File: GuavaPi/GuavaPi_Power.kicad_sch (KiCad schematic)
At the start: 1 part

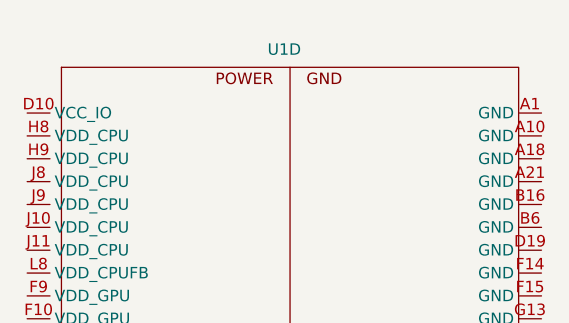
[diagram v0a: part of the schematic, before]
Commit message: Started DRAM Design
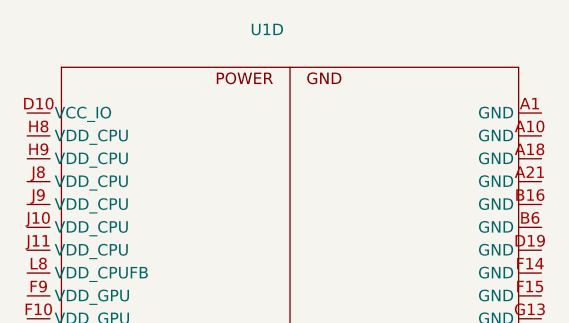
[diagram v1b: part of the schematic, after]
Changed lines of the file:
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@@
   (symbol (lib_id "Allwinner_H616:Allwinner_H616") (at 17.272 19.558 0) (unit 4)
     (in_bom yes) (on_board yes) (dnp no) (fields_autoplaced)
-    (property "Reference" "U1" (at 56.007 23.9268 0)
+    (property "Reference" "U1" (at 54.102 21.7424 0)
       (effects (font (size 1.27 1.27)))
     )
@@
           (reference "U1") (unit 4)
         )
+        (path "/3be7235b-2d12-456d-bbdb-dcc9c2ae1afd/dc1a4d83-a933-4336-ba01-88286996a5dc"
+          (reference "U1") (unit 4)
+        )

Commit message: AXP313A
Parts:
- added C38, C39, C40, C42, C45: 4.7uF, symbol Device:C
- added C41: 1uF, symbol Device:C
- added C43, C44, C46, C47, C48, C49, C50: 22uF, symbol Device:C
- added L1, L2, L3: 1uH, symbol Device:L
- added R10, R11, R12, R13: 2k, symbol Device:R
- added R9: 510R, symbol Device:R
- added UP1: ~, symbol allwinner_h616:AXP313A
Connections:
- new net: C40.2, R9.1, UP1.7 (RTCLCO)
- new net: L1.1, UP1.18 (LX1)
- new net: R12.1, UP1.11 (IRQ)
- new net: L2.1, UP1.19 (LX2)
- new net: C41.2, UP1.8 (GPO)
- new net: C42.1, UP1.17 (VIN1)
- new net: R13.1, UP1.13 (PWROK)
- new net 1V8: C38.2, R10.2, R11.2, UP1.15 (ALDO1)
- new net 3V3: C39.2, UP1.12 (DLDO1)
- new net GND: C38.1, C39.1, C40.1, C41.1, C42.2, C43.2, C44.2, C45.2, C46.2, C47.2, C48.2, C49.2, C50.2, R9.2, UP1.21 (EPAD), UP1.4 (GND)
- new net IRQ: R12.2
- new net PMU_SCK: R11.1, UP1.6 (SCL)
- new net PMU_SDA: R10.1, UP1.5 (SDA)
- new net PS: C45.1, C48.1, UP1.20 (VIN2)
- new net RESET: R13.2
- new net VCC_DRAM: C49.1, C50.1, L3.2
- new net VDD_CPU: C46.1, C47.1, L2.2, UP1.1 (DCDC2)
- new net VDD_GPU: C43.1, C44.1, L1.2, UP1.16 (DCDC1)
- no-connect marks 0 -> 2

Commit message: Power H616
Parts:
- added C51, C52, C53, C54, C55, C56, C57, C58, C59, C60, C61, C62, C63, C64, C65, C66, C67: 100nF, symbol Device:C
- added D1: LED, symbol Device:LED
- added D2: D, symbol Device:D
- added J1: 0533980271, MOLEX_0533980271, symbol 0533980271:0533980271
- added R14: 10k, symbol Device:R
- added R15: 5k1, symbol Device:R
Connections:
- net VCC_DRAM is gone; now on net VCC-DRAM: C49.1, C50.1, L3.2
- net VDD_CPU is gone; now on net VDD-CPU: C46.1, C47.1, L2.2, UP1.1 (DCDC2)
- net VDD_GPU is gone; now on net VDD-GPU: C43.1, C44.1, L1.2, UP1.16 (DCDC1)
- net 1V8: now also C52.2, C53.2, C54.2, R14.1
- net 3V3: now also C59.2, C60.2, C61.2, C62.2, R15.1
- net GND: now also U1.A1 (GND1), U1.A10 (GND2), U1.A18 (GND3), U1.A21 (GND4), U1.B16 (GND6), U1.B6 (GND5), U1.D19 (GND7), U1.F14 (GND8), U1.F15 (GND9), U1.G13 (GND10), U1.G14 (GND11), U1.G15 (GND12), U1.H10 (GND13), U1.H11 (GND14), U1.H12 (GND15), U1.H13 (GND16), U1.H14 (GND17), U1.H15 (GND18), U1.H19 (GND19), U1.J12 (GND20), U1.J13 (GND21), U1.J14 (GND22), U1.J15 (GND23), U1.K10 (GND26), U1.K11 (GND27), U1.K12 (GND28), U1.K13 (GND29), U1.K14 (GND30), U1.K15 (GND31), U1.K8 (GND24), U1.K9 (GND25), U1.L21 (GND32), U1.M1 (GND33), U1.M2 (GND34), U1.M3 (GND35), U1.N12 (GND38), U1.N15 (GND39), U1.N18 (GND40), U1.N6 (GND36), U1.N9 (GND37), U1.P3 (GND41), U1.R21 (GND43), U1.R5 (GND42), U1.T1 (GND44), U1.T10 (GND47), U1.T15 (GND48), U1.T17 (GND49), U1.T3 (GND45), U1.T8 (GND46), U1.U13 (GND51), U1.U6 (GND50), U1.V1 (GND52), U1.V12 (GND54), U1.V19 (GND55), U1.V21 (GND56), U1.V5 (GND53), C51.1, C52.1, C53.1, C54.1, C55.1, C56.1, C57.1, C58.1, C59.1, C60.1, C61.1, C62.1, C63.1, C64.1, C65.1, C66.1, C67.1, D1.1 (K), J1.2, J1.S1 (SHIELD), J1.S2 (SHIELD__1)
- net PS: now also UP1.2 (VIN3), D2.2 (A)
- net RESET: now also C51.2, R14.2
- net +3.3V: now reaches U1.D10 (VCC_IO)
- net VDD-GPU: now reaches U1.F10 (VDD_GPU2)
- net VDD-GPU: now also U1.F11 (VDD_SYS1), U1.F12 (VDD_SYS2), U1.F13 (VDD_SYS3), U1.F8 (VDD_GPUFB), U1.F9 (VDD_GPU1), U1.G10 (VDD_SYS4), U1.G11 (VDD_SYS5), U1.G12 (VDD_SYS6), U1.G8 (VDD_GPU3), U1.G9 (VDD_GPU4), C63.2, C64.2, C65.2
- net VDD-CPU: now reaches U1.H8 (VDD_CPU1)
- net VDD-CPU: now also U1.H9 (VDD_CPU2), U1.J10 (VDD_CPU5), U1.J11 (VDD_CPU6), U1.J8 (VDD_CPU3), U1.J9 (VDD_CPU4), U1.L8 (VDD_CPUFB), C66.2, C67.2
- net at UP1.3 (LX3): now also L3.1
- net VCC-DRAM: now reaches UP1.4 (GND)
- net VCC-DRAM: now also C55.2, C56.2, C57.2, C58.2
- new net: D2.1 (K), J1.1
- new net: D1.2 (A), R15.2

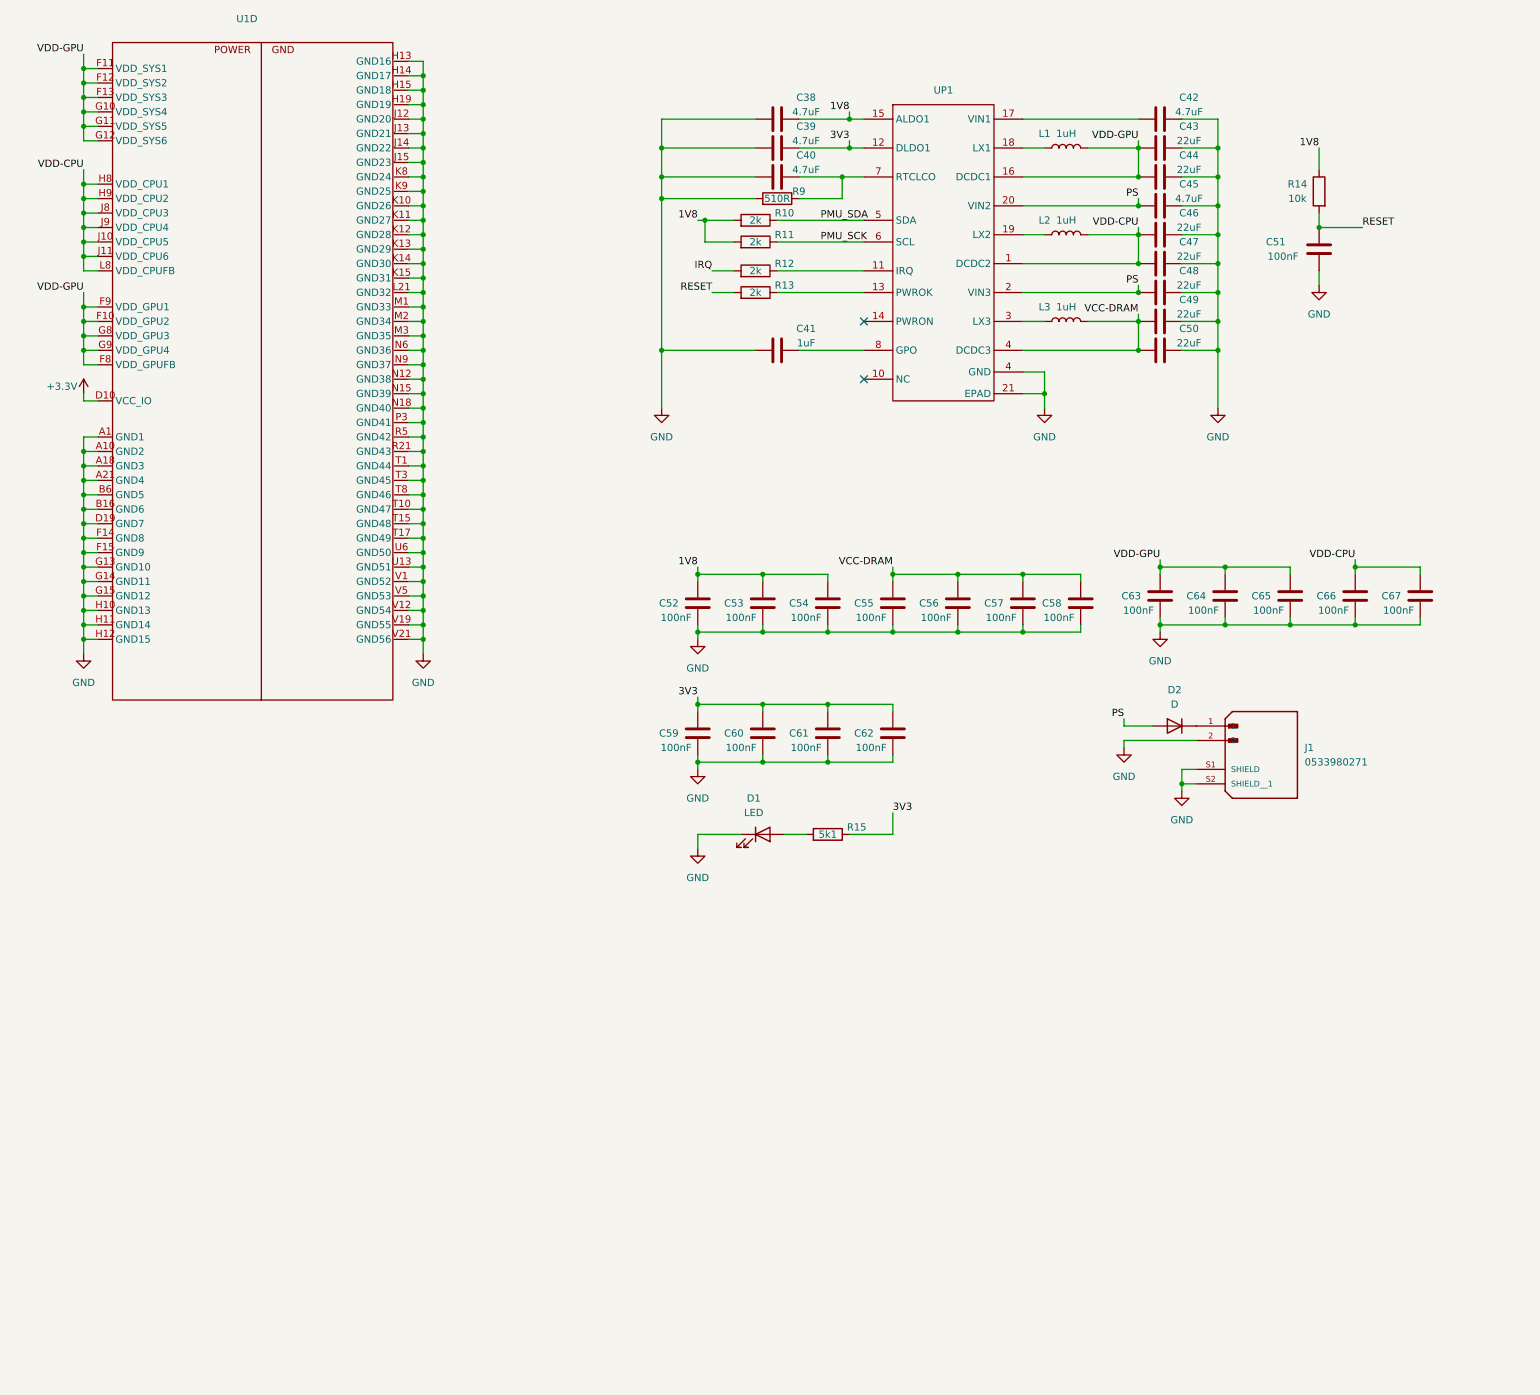
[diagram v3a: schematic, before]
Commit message: Added USB-C
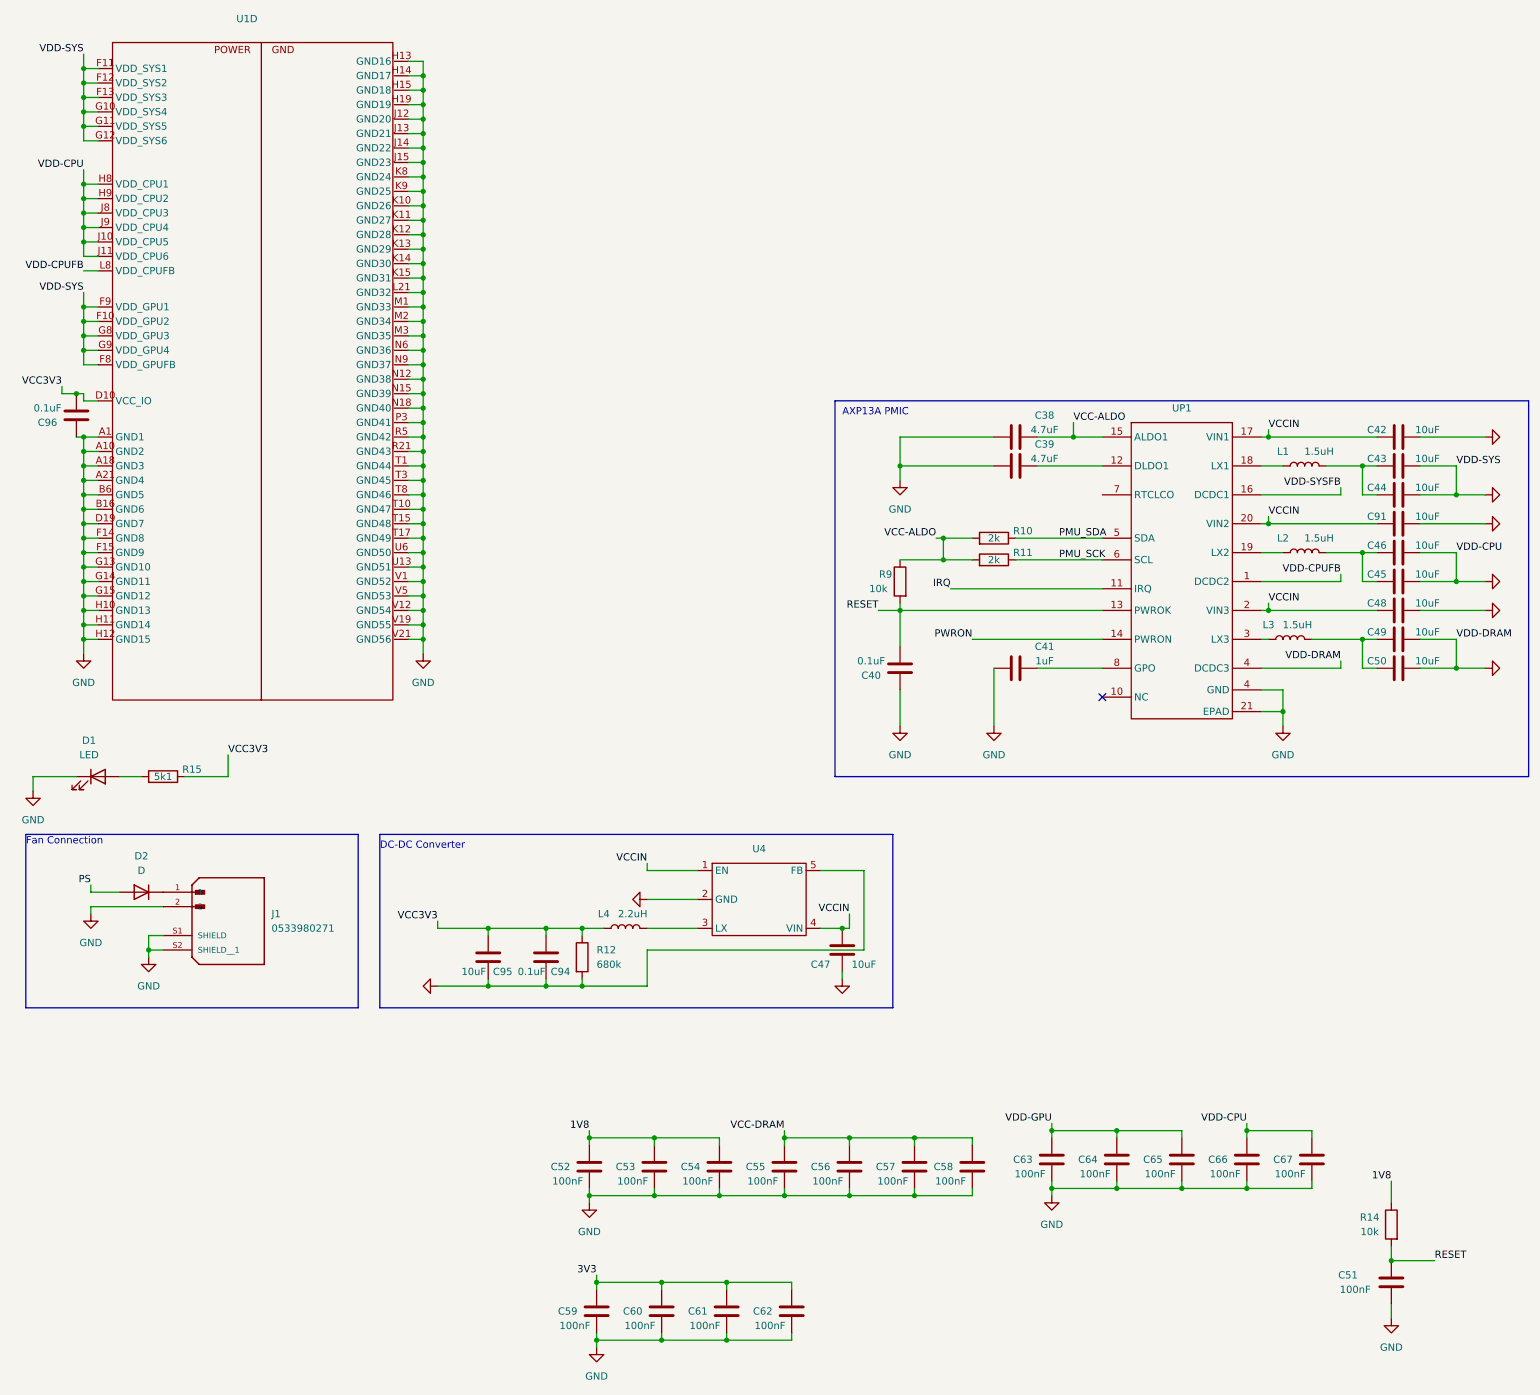
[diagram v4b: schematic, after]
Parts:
- removed R13: 2k, symbol Device:R
- added C91, C95: 10uF, symbol Device:C
- added C94, C96: 0.1uF, symbol Device:C
- added L4: 2.2uH, symbol Device:L
- added U4: ~, symbol Converter_DCDC:MT3410LB
- C40: value 4.7uF -> 0.1uF
- C42, C45: value 4.7uF -> 10uF
- C43, C44, C46, C47, C48, C49, C50: value 22uF -> 10uF
- L1, L2, L3: value 1uH -> 1.5uH
- R12: value 2k -> 680k
- R9: value 510R -> 10k
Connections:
- net +3.3V is gone; now on net VCC3V3: U1.D10 (VCC_IO)
- net 1V8: no longer C38.2, R10.2, R11.2, UP1.15 (ALDO1)
- net 3V3: no longer C39.2, R15.1, UP1.12 (DLDO1)
- net GND: now also C47.1, C66.2, C67.2, R12.2, U1.F10 (VDD_GPU2), U1.F11 (VDD_SYS1), U1.F12 (VDD_SYS2), U1.F13 (VDD_SYS3), U1.F8 (VDD_GPUFB), U1.F9 (VDD_GPU1), U1.G10 (VDD_SYS4), U1.G11 (VDD_SYS5), U1.G12 (VDD_SYS6), U1.G8 (VDD_GPU3), U1.G9 (VDD_GPU4), U1.H8 (VDD_CPU1), U1.H9 (VDD_CPU2), U1.J10 (VDD_CPU5), U1.J11 (VDD_CPU6), U1.J8 (VDD_CPU3), U1.J9 (VDD_CPU4), C91.2, C94.1, C95.1, C96.1, U4.2 (GND), U4.5 (FB); no longer C47.2, R9.2
- net IRQ: now also UP1.11 (IRQ); no longer R12.2
- net PS: no longer C45.1, C48.1, UP1.2 (VIN3), UP1.20 (VIN2)
- net RESET: now also C40.2, R9.2, UP1.13 (PWROK)
- net VCC-DRAM: no longer C49.1, C50.1, L3.2, UP1.4 (GND)
- net VDD-GPU: no longer C43.1, C44.1, L1.2, U1.F10 (VDD_GPU2), U1.F11 (VDD_SYS1), U1.F12 (VDD_SYS2), U1.F13 (VDD_SYS3), U1.F8 (VDD_GPUFB), U1.F9 (VDD_GPU1), U1.G10 (VDD_SYS4), U1.G11 (VDD_SYS5), U1.G12 (VDD_SYS6), U1.G8 (VDD_GPU3), U1.G9 (VDD_GPU4), UP1.16 (DCDC1)
- net VCC3V3: now reaches R12.1
- net VCC3V3: now also R15.1, C94.2, C95.2, C96.2, L4.1; no longer UP1.11 (IRQ)
- net VCCIN: now reaches C42.1, UP1.17 (VIN1)
- net VCCIN: now also C47.2, C48.1, UP1.2 (VIN3), UP1.20 (VIN2), C91.1, U4.1 (EN), U4.4 (VIN)
- net PWRON: now reaches UP1.14 (PWRON)
- removed net VDD-CPU: C46.1, C47.1, C66.2, C67.2, L2.2, U1.H8 (VDD_CPU1), U1.H9 (VDD_CPU2), U1.J10 (VDD_CPU5), U1.J11 (VDD_CPU6), U1.J8 (VDD_CPU3), U1.J9 (VDD_CPU4), U1.L8 (VDD_CPUFB), UP1.1 (DCDC2)
- new net: C39.2, UP1.12 (DLDO1)
- new net: C43.1, C44.1, L1.2
- new net: C45.1, C46.1, L2.2
- new net: L4.2, U4.3 (LX)
- new net: C49.1, C50.1, L3.2
- new net VCC-ALDO: C38.2, R10.2, R11.2, R9.1, UP1.15 (ALDO1)
- new net VDD-CPUFB: U1.L8 (VDD_CPUFB), UP1.1 (DCDC2)
- new net VDD-SYSFB: UP1.16 (DCDC1)
- now unconnected: UP1.7 (RTCLCO)
- no-connect marks 2 -> 1
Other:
- note added: "AXP13A PMIC"
- note added: "DC-DC Converter"
- note added: "Fan Connection"
- moved on the sheet: C38, C39, C41, C42, C43, C44, C46, C48, C49, C50, C51, C52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
